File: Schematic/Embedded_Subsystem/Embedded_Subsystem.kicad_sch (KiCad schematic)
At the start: 11 parts, among them J1 Micro_SD_Card, J10 Conn_01x06, J11 Conn_01x04, J2 Conn_01x04, J3 Conn_01x07, J4 Conn_01x04, J5 Conn_01x09, J6 Conn_01x19, J7 Conn_01x19, J8 Conn_01x04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

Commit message: Labeled some STM GPIO pins, added I2C and SPI connections.
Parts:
- removed J6, J7: Conn_01x19, symbol Connector_Generic:Conn_01x19
- added J12, J7: Conn_01x20, symbol Connector_Generic:Conn_01x20
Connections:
- net +3V3: now also J12.3 (Pin_3), J7.20 (Pin_20)
- net +5V: now also J12.1 (Pin_1), J7.18 (Pin_18)
- net GND: now also J12.2 (Pin_2), J7.19 (Pin_19)
- net Link_NRST: now also J12.15 (Pin_15)
- net SCK_1 renamed I2C1_SCK
- net I2C1_SCK: now also J7.14 (Pin_14)
- net SCK_2 renamed I2C2_SCK
- net I2C2_SCK: now also J12.4 (Pin_4)
- net SCK_3 renamed I2C3_SCK
- net I2C3_SCK: now also J7.5 (Pin_5)
- net SDA_1 renamed I2C1_SDA
- net I2C1_SDA: now also J7.15 (Pin_15)
- net SDA_2 renamed I2C2_SDA
- net I2C2_SDA: now also J7.11 (Pin_11)
- net SDA_3 renamed I2C3_SDA
- net I2C3_SDA: now also J7.12 (Pin_12)
- new net SPI1_MISO: J12.9 (Pin_9)
- new net SPI1_MOSI: J12.8 (Pin_8)
- new net SPI1_SCK: J12.10 (Pin_10)

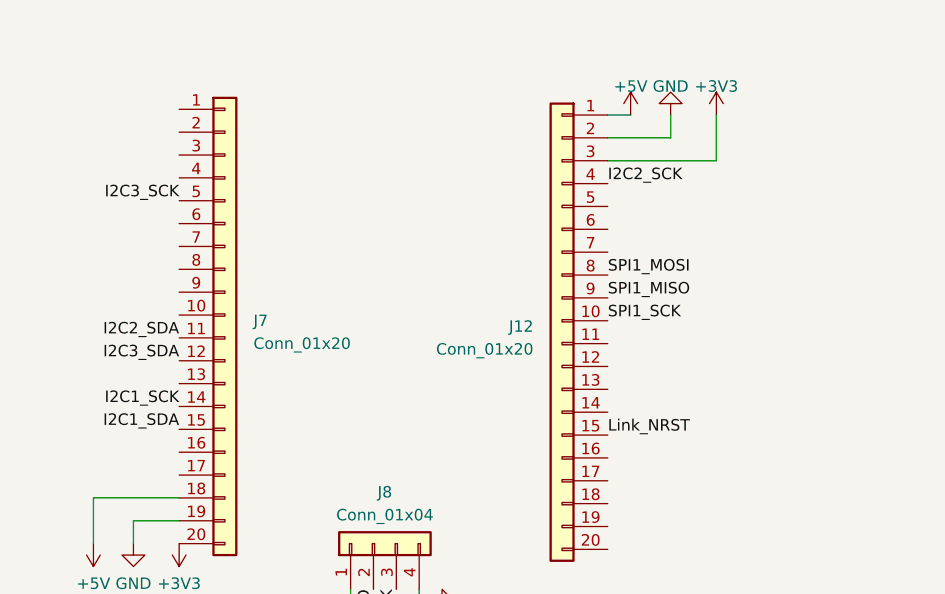
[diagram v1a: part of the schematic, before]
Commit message: Generating MX code for SD Card Interface
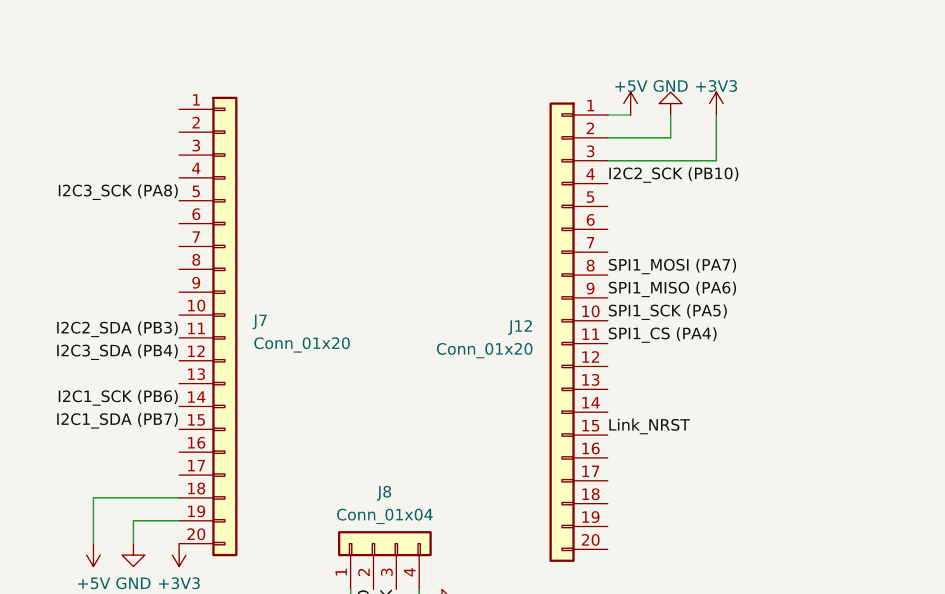
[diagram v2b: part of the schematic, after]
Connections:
- net I2C1_SCK: no longer J7.14 (Pin_14)
- net I2C1_SDA: no longer J7.15 (Pin_15)
- net I2C2_SCK: no longer J12.4 (Pin_4)
- net I2C2_SDA: no longer J7.11 (Pin_11)
- net I2C3_SCK: no longer J7.5 (Pin_5)
- net I2C3_SDA: no longer J7.12 (Pin_12)
- net SPI1_CS (PA4): now reaches J12.11 (Pin_11)
- net SPI1_MISO renamed SPI1_MISO (PA6)
- net SPI1_MOSI renamed SPI1_MOSI (PA7)
- net SPI1_SCK renamed SPI1_SCK (PA5)
- new net I2C1_SCK (PB6): J7.14 (Pin_14)
- new net I2C1_SDA (PB7): J7.15 (Pin_15)
- new net I2C2_SCK (PB10): J12.4 (Pin_4)
- new net I2C2_SDA (PB3): J7.11 (Pin_11)
- new net I2C3_SCK (PA8): J7.5 (Pin_5)
- new net I2C3_SDA (PB4): J7.12 (Pin_12)
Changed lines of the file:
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@@
     (effects (font (size 1.27 1.27)) (justify right bottom))
   )
-  (label "I2C1_SCK" (at 41.275 158.115 180) (fields_autoplaced)
+  (label "I2C1_SCK (PB6)" (at 41.275 158.115 180) (fields_autoplaced)
     (effects (font (size 1.27 1.27)) (justify right bottom))
+  )
+  (label "SPI1_CS (PA4)" (at 88.9 151.13 0) (fields_autoplaced)
+    (effects (font (size 1.27 1.27)) (justify left bottom))
   )
   (label "DAT1{slash}!IRQ" (at 230.505 88.265 0) (fields_autoplaced)
@@
     (effects (font (size 1.27 1.27)) (justify right bottom))
   )
-  (label "I2C3_SCK" (at 41.275 135.255 180) (fields_autoplaced)
+  (label "I2C3_SCK (PA8)" (at 41.275 135.255 180) (fields_autoplaced)
     (effects (font (size 1.27 1.27)) (justify right bottom))
   )
-  (label "I2C2_SCK" (at 88.9 133.35 0) (fields_autoplaced)
+  (label "I2C2_SCK (PB10)" (at 88.9 133.35 0) (fields_autoplaced)
     (effects (font (size 1.27 1.27)) (justify left bottom))
   )
-  (label "I2C2_SDA" (at 41.275 150.495 180) (fields_autoplaced)
+  (label "I2C2_SDA (PB3)" (at 41.275 150.495 180) (fields_autoplaced)
     (effects (font (size 1.27 1.27)) (justify right bottom))
   )
-  (label "SPI1_MISO" (at 88.9 146.05 0) (fields_autoplaced)
+  (label "SPI1_MISO (PA6)" (at 88.9 146.05 0) (fields_autoplaced)
     (effects (font (size 1.27 1.27)) (justify left bottom))
   )
-  (label "I2C1_SDA" (at 41.275 160.655 180) (fields_autoplaced)
+  (label "I2C1_SDA (PB7)" (at 41.275 160.655 180) (fields_autoplaced)
     (effects (font (size 1.27 1.27)) (justify right bottom))
   )
-  (label "I2C3_SDA" (at 41.275 153.035 180) (fields_autoplaced)
+  (label "I2C3_SDA (PB4)" (at 41.275 153.035 180) (fields_autoplaced)
     (effects (font (size 1.27 1.27)) (justify right bottom))
   )
-  (label "SPI1_MOSI" (at 88.9 143.51 0) (fields_autoplaced)
+  (label "SPI1_MOSI (PA7)" (at 88.9 143.51 0) (fields_autoplaced)
     (effects (font (size 1.27 1.27)) (justify left bottom))
   )
@@
     (effects (font (size 1.27 1.27)) (justify right bottom))
   )
-  (label "SPI1_SCK" (at 88.9 148.59 0) (fields_autoplaced)
+  (label "SPI1_SCK (PA5)" (at 88.9 148.59 0) (fields_autoplaced)
     (effects (font (size 1.27 1.27)) (justify left bottom))
   )

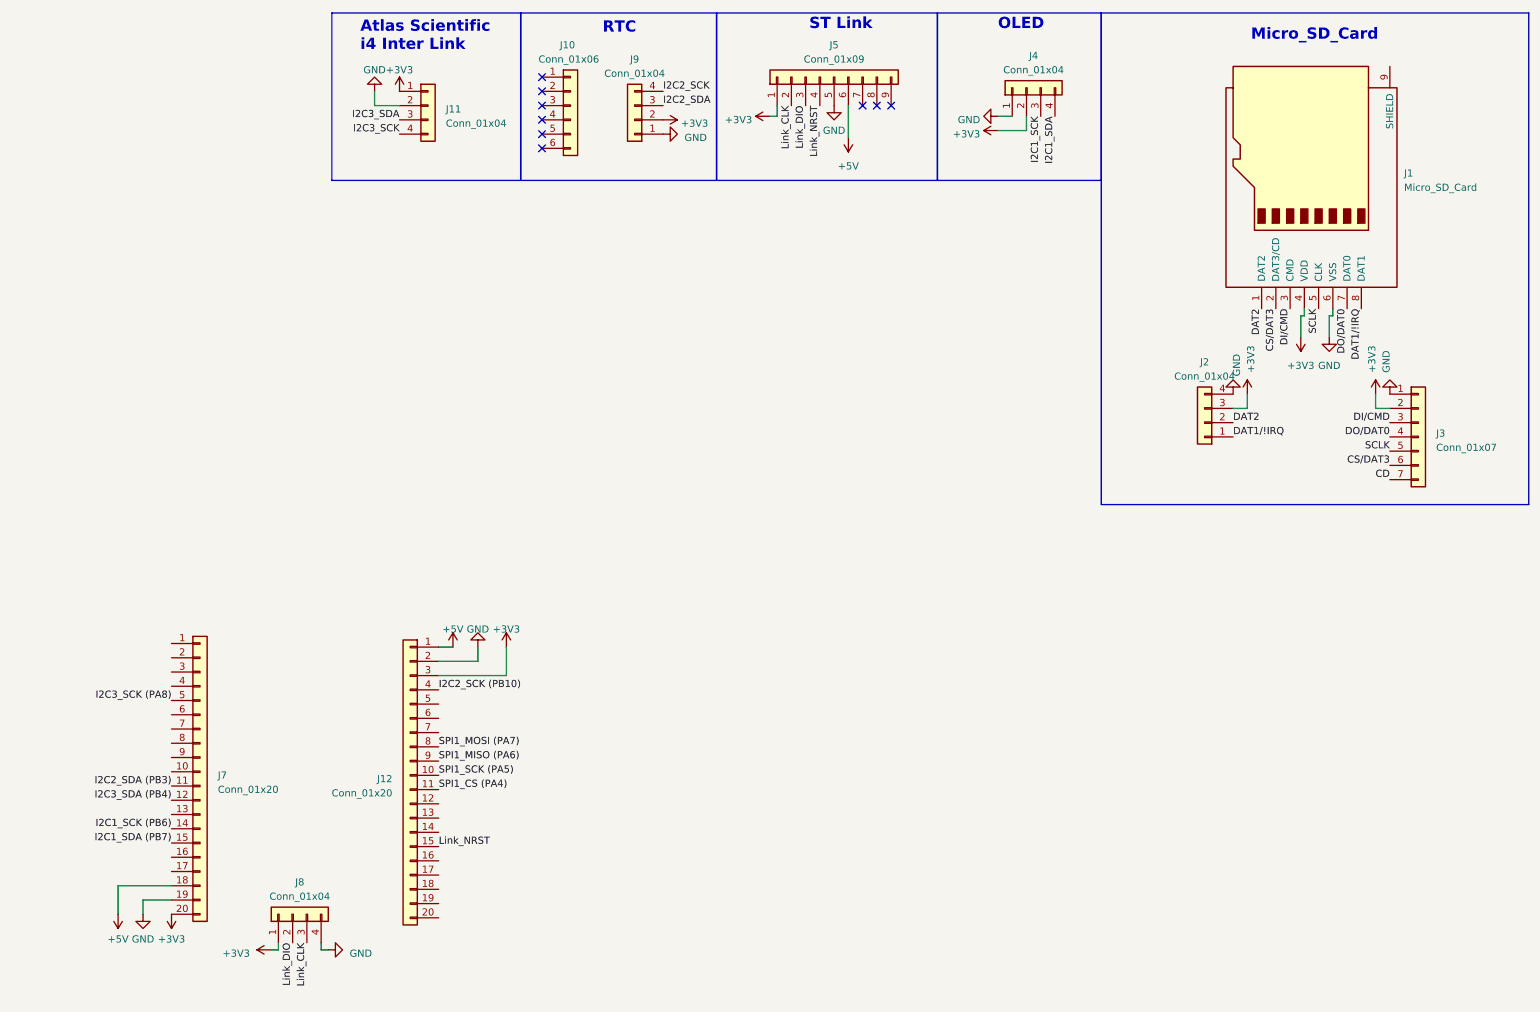
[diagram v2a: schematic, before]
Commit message: Found Lora SX1278 Library. Added to SRC and INC.
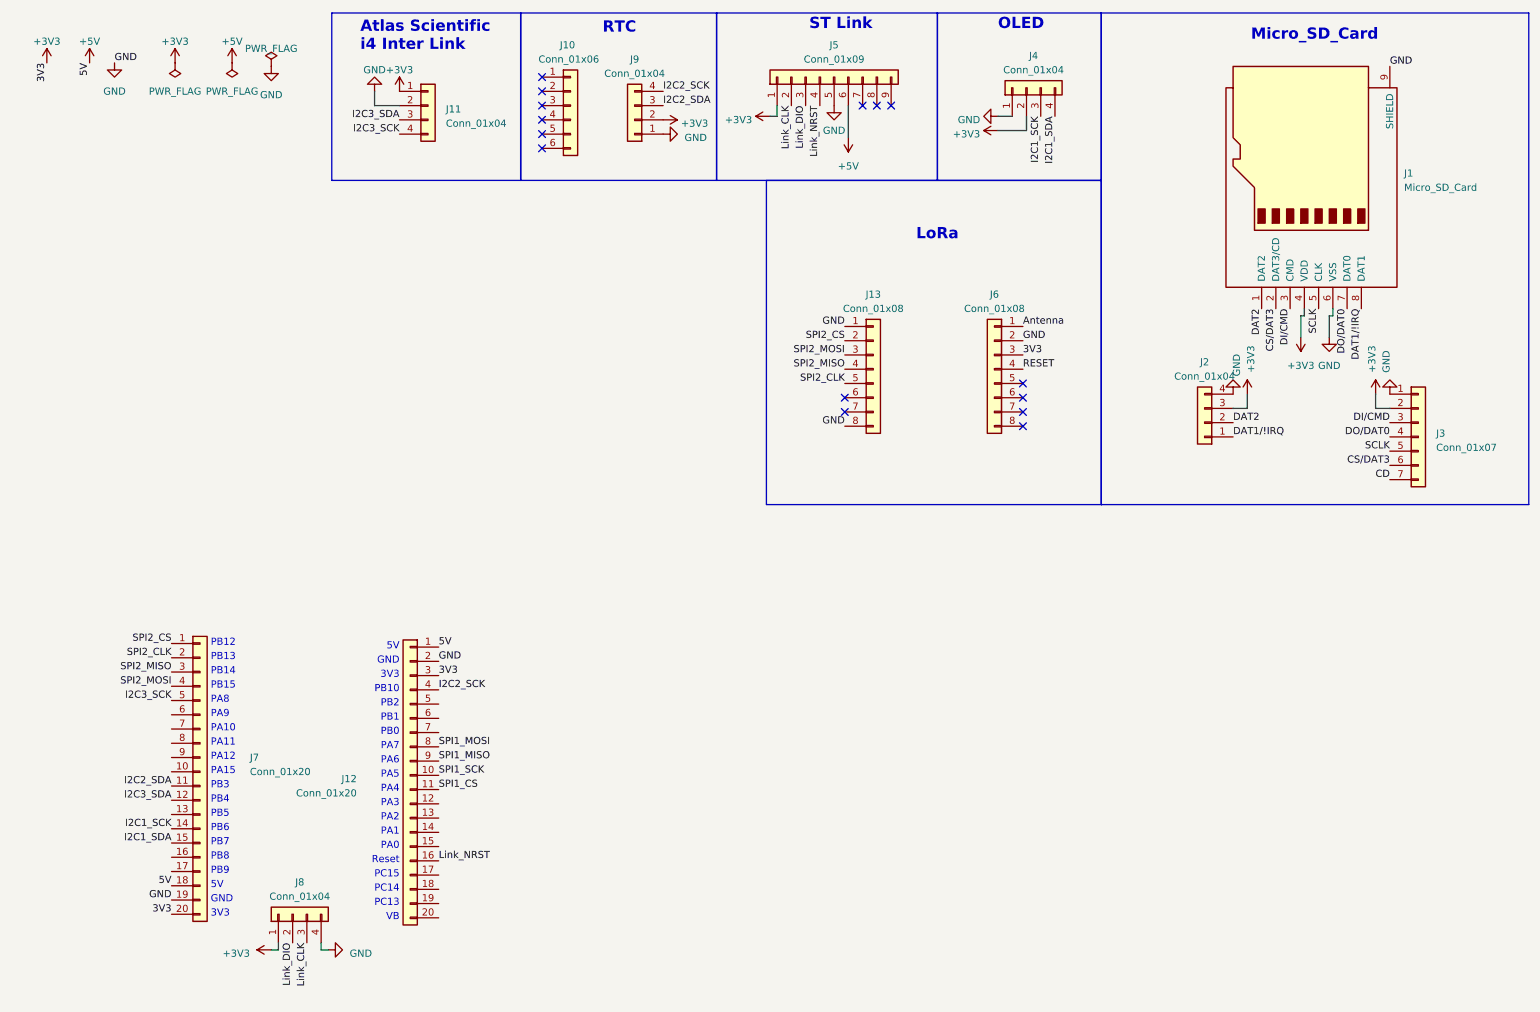
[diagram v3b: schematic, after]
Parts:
- added J13, J6: Conn_01x08, symbol Connector_Generic:Conn_01x08
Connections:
- net I2C1_SCK (PB6) is gone; now on net I2C1_SCK: J7.14 (Pin_14)
- net I2C1_SDA (PB7) is gone; now on net I2C1_SDA: J7.15 (Pin_15)
- net I2C2_SCK (PB10) is gone; now on net I2C2_SCK: J12.4 (Pin_4)
- net I2C2_SDA (PB3) is gone; now on net I2C2_SDA: J7.11 (Pin_11)
- net I2C3_SCK (PA8) is gone; now on net I2C3_SCK: J7.5 (Pin_5)
- net I2C3_SDA (PB4) is gone; now on net I2C3_SDA: J7.12 (Pin_12)
- net +3V3: now also J6.3 (Pin_3)
- net GND: now also J1.9 (SHIELD), J13.1 (Pin_1), J13.8 (Pin_8), J6.2 (Pin_2)
- net Link_NRST: now also J12.16 (Pin_16); no longer J12.15 (Pin_15)
- net SPI2_CS: now reaches J7.1 (Pin_1)
- net SPI2_CS: now also J13.2 (Pin_2)
- net SPI2_CLK: now reaches J7.2 (Pin_2)
- net SPI2_CLK: now also J13.5 (Pin_5)
- net SPI2_MISO: now reaches J7.3 (Pin_3)
- net SPI2_MISO: now also J13.4 (Pin_4)
- net SPI2_MOSI: now reaches J7.4 (Pin_4)
- net SPI2_MOSI: now also J13.3 (Pin_3)
- net SPI1_CS (PA4) renamed SPI1_CS
- net SPI1_MISO (PA6) renamed SPI1_MISO
- net SPI1_MOSI (PA7) renamed SPI1_MOSI
- net SPI1_SCK (PA5) renamed SPI1_SCK
- new net Antenna: J6.1 (Pin_1)
- new net RESET: J6.4 (Pin_4)
- no-connect marks 9 -> 15
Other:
- note added: "3V3"
- note added: "5V"
- note added: "GND"
- note added: "LoRa"
- note added: "PA0"
- note added: "PA1"
- note added: "PA10"
- note added: "PA11"
- note added: "PA12"
- note added: "PA15"
- note added: "PA2"
- note added: "PA3"
- note added: "PA4"
- note added: "PA5"
- note added: "PA6"
- note added: "PA7"
- note added: "PA8"
- note added: "PA9"
- note added: "PB0"
- note added: "PB1"
- note added: "PB10"
- note added: "PB12"
- note added: "PB13"
- note added: "PB14"
- note added: "PB15"
- note added: "PB2"
- note added: "PB3"
- note added: "PB4"
- note added: "PB5"
- note added: "PB6"
- note added: "PB7"
- note added: "PB8"
- note added: "PB9"
- note added: "PC13"
- note added: "PC14"
- note added: "PC15"
- note added: "Reset"
- note added: "VB"

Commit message: Added Atlas Read Code
Added code to read from an Atlas scientific sensor board.

Successfully reading and displaying DO and RTD for 1 sensor.

Also added code to respond to battery command with dummy response.
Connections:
- net CS/DAT3: no longer J3.6 (Pin_6)
- net DI/CMD: no longer J3.3 (Pin_3)
- net DO/DAT0: no longer J3.4 (Pin_4)
- net SCLK: no longer J3.5 (Pin_5)
- net SPI1_MISO: now also J3.4 (Pin_4)
- net SPI1_MOSI: now also J3.3 (Pin_3)
- net SPI1_CS renamed SD_CS
- net SD_CS: now also J3.6 (Pin_6)
- new net SPI1_CLK: J3.5 (Pin_5)
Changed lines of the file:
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@@
     (effects (font (size 1.27 1.27)) (justify right bottom))
   )
-  (label "DO{slash}DAT0" (at 258.445 88.265 180) (fields_autoplaced)
+  (label "SPI1_MISO" (at 258.445 88.265 180) (fields_autoplaced)
     (effects (font (size 1.27 1.27)) (justify right bottom))
   )
@@
     (effects (font (size 1.27 1.27)) (justify left bottom))
   )
-  (label "DI{slash}CMD" (at 258.445 85.725 180) (fields_autoplaced)
+  (label "SPI1_MOSI" (at 258.445 85.725 180) (fields_autoplaced)
     (effects (font (size 1.27 1.27)) (justify right bottom))
   )
@@
     (effects (font (size 1.27 1.27)) (justify right bottom))
   )
-  (label "SPI1_CS" (at 88.9 151.13 0) (fields_autoplaced)
+  (label "SD_CS" (at 88.9 151.13 0) (fields_autoplaced)
     (effects (font (size 1.27 1.27)) (justify left bottom))
   )
@@
     (effects (font (size 1.27 1.27)) (justify left bottom))
   )
-  (label "CS{slash}DAT3" (at 258.445 93.345 180) (fields_autoplaced)
+  (label "SD_CS" (at 258.445 93.345 180) (fields_autoplaced)
     (effects (font (size 1.27 1.27)) (justify right bottom))
   )
-  (label "SCLK" (at 258.445 90.805 180) (fields_autoplaced)
+  (label "SPI1_CLK" (at 258.445 90.805 180) (fields_autoplaced)
     (effects (font (size 1.27 1.27)) (justify right bottom))
   )

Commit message: Fixed MX issue that disabled LFN for SD card
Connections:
- net CD is gone; now on net SD_CD: J3.7 (Pin_7)
- net SD_CD: now reaches J12.12 (Pin_12)
